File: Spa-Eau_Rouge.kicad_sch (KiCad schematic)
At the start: 8 parts, among them J1 XT30PW-M, J2 PH1RA-03-UA, J3 SM02B-GHS-TB, J4 1985807

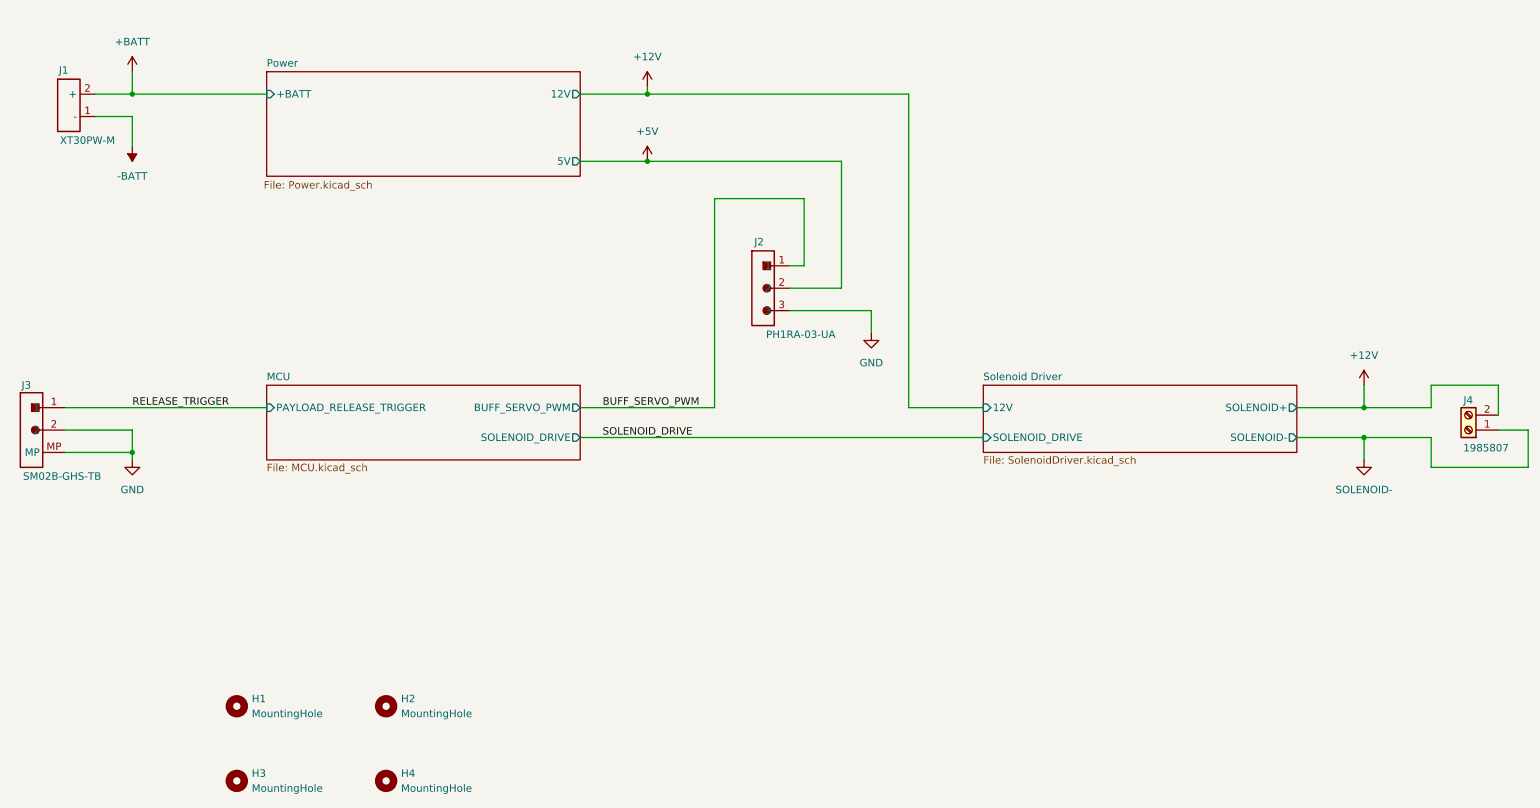
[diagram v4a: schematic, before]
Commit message: added i2c + another servo rail
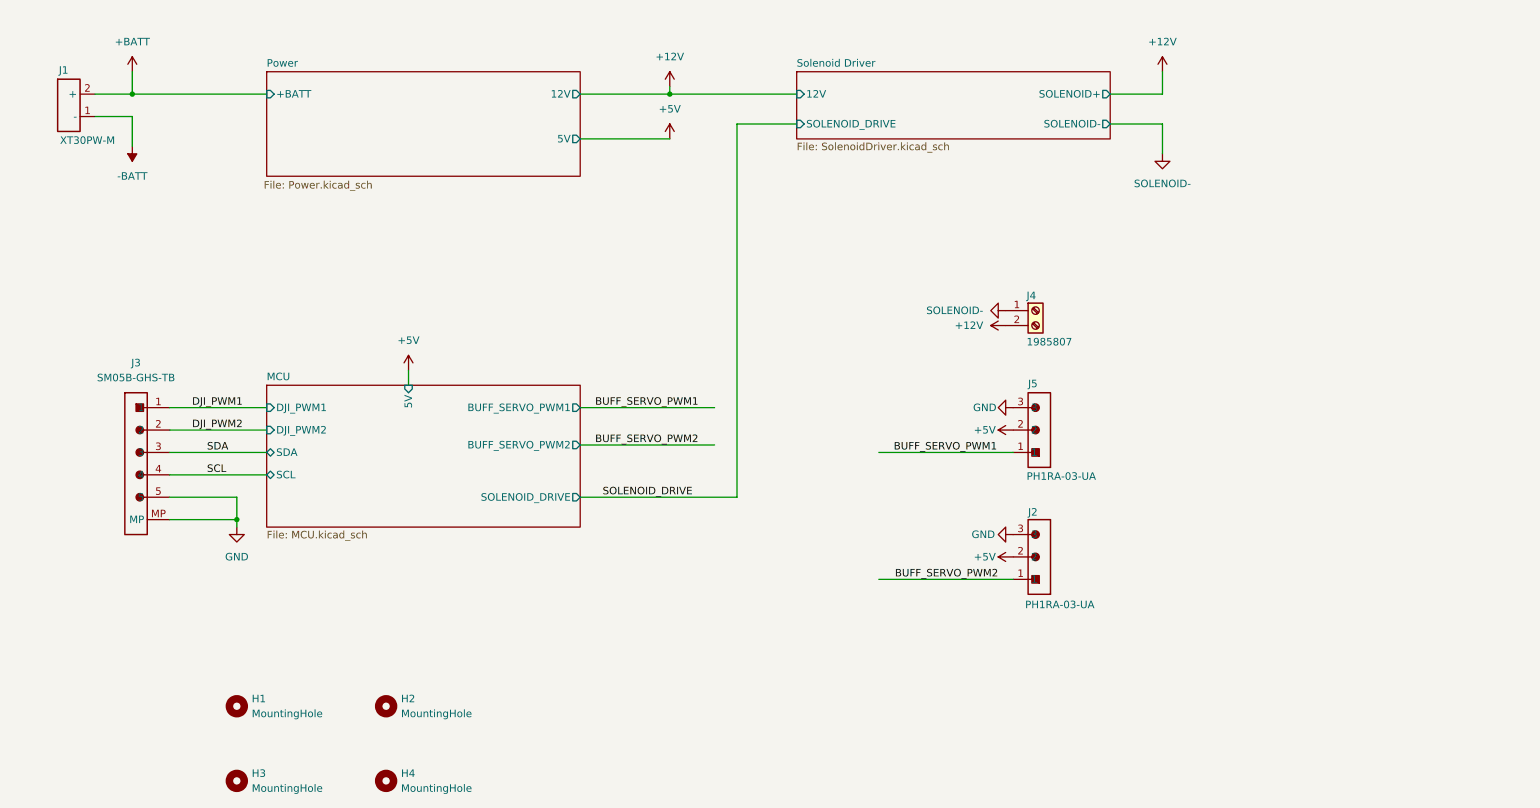
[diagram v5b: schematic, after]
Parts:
- removed J3: SM02B-GHS-TB, Connector_JST:JST_GH_SM02B-GHS-TB_1x02-1MP_P1.25mm_Horizontal, symbol Connector:JST-GH_SM02B-GHS-TB
- added J3: SM05B-GHS-TB, Connector_JST:JST_GH_SM05B-GHS-TB_1x05-1MP_P1.25mm_Horizontal, symbol Connector:JST-GH_SM05B-GHS-TB
- added J5: PH1RA-03-UA, Connector_PinHeader_2.54mm:PinHeader_1x03_P2.54mm_Horizontal, symbol Connector:Conn-1x03-2.54mm-RA_PH1RA-03-UA
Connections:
- net +5V: now also J5.2
- net GND: now also J3.5, J3.MP, J5.3
- net BUFF_SERVO_PWM renamed BUFF_SERVO_PWM2
- new net BUFF_SERVO_PWM1: J5.1
- new net DJI_PWM1: J3.1
- new net DJI_PWM2: J3.2
- new net SCL: J3.4
- new net SDA: J3.3
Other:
- sheet MCU ports: added 5V, BUFF_SERVO_PWM1, BUFF_SERVO_PWM2, DJI_PWM1, DJI_PWM2, SCL, SDA; removed BUFF_SERVO_PWM, PAYLOAD_RELEASE_TRIGGER
- moved on the sheet: J4

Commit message: 2nd rev is done
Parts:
- removed J2: PH1RA-03-UA, Connector_PinHeader_2.54mm:PinHeader_1x03_P2.54mm_Horizontal, symbol Connector:Conn-1x03-2.54mm-RA_PH1RA-03-UA
- added J5: PH1RA-03-UA, Connector_PinHeader_2.54mm:PinHeader_1x03_P2.54mm_Horizontal, symbol Connector:Conn-1x03-2.54mm-RA_PH1RA-03-UA
- renumbered J3 to J2, J4 to J3, J5 to J4
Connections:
- net +12V: now also J3.1 (Pin_1); no longer J3.2 (Pin_2)
- net +5V: now also J5.2
- net BUFF_SERVO_PWM2: now also J5.1
- net GND: now also J5.3
- net SOLENOID-: now also J3.2 (Pin_2); no longer J3.1 (Pin_1)
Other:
- sheet MCU ports: added VIN_LED; removed none
- sheet Power ports: added VIN_LED; removed none
- moved on the sheet: J2, J3, J4
